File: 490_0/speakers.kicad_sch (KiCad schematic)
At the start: 14 parts, among them U1 MAX98357A, U2 MAX98357A

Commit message: Minor updates
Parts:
- renumbered FB1 to FB2, FB2 to FB3, R1 to R48, R2 to R49, U2 to U10, U1 to U9

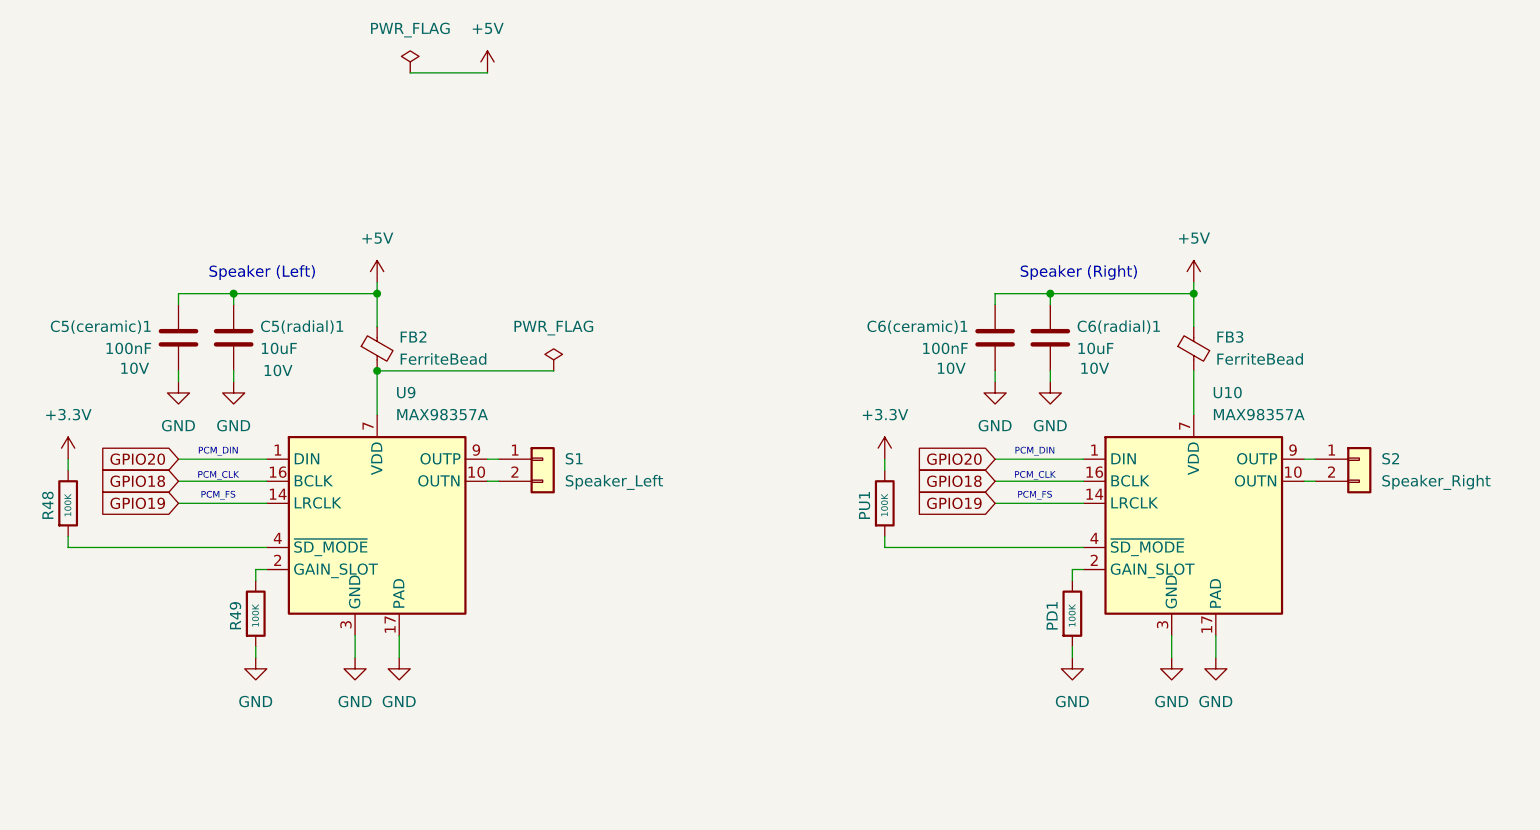
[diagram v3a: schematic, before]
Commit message: Updated box diagram
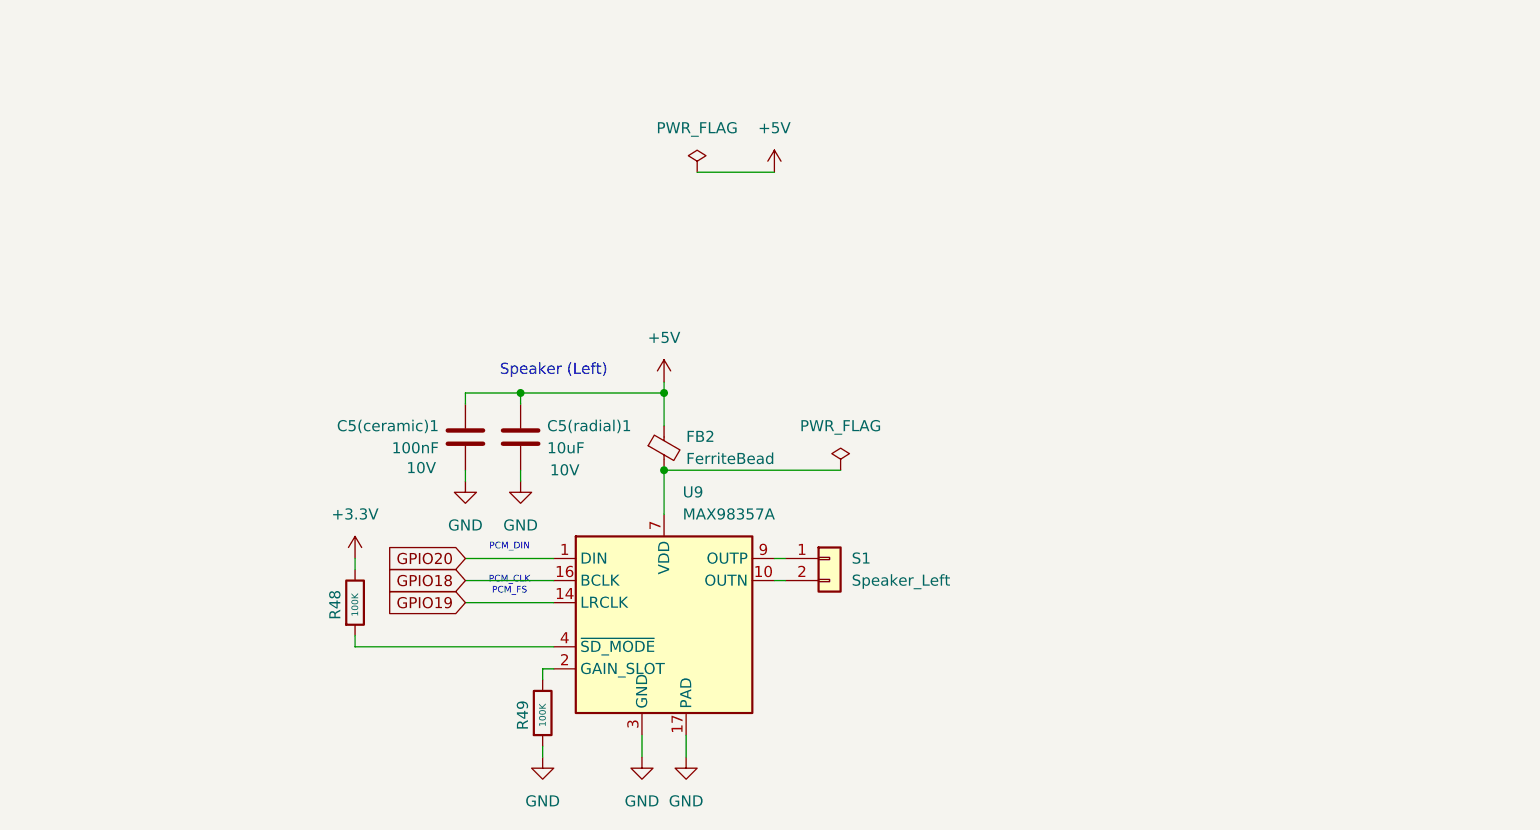
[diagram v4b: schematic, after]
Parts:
- removed C6(ceramic)1: 100nF, Capacitor_SMD:C_0603_1608Metric, symbol Device:C
- removed C6(radial)1: 10uF, Capacitor_THT:CP_Radial_D5.0mm_P2.50mm, symbol Device:C
- removed FB3: FerriteBead, Capacitor_SMD:C_0603_1608Metric, symbol Device:FerriteBead_Small
- removed PD1, PU1: 100K, symbol Device:R
- removed S2: Speaker_Right, Connector_JST:JST_PH_S2B-PH-K_1x02_P2.00mm_Horizontal, symbol Connector_Generic:Conn_01x02
- removed U10: MAX98357A, Package_DFN_QFN:TQFN-16-1EP_3x3mm_P0.5mm_EP1.23x1.23mm_ThermalVias, symbol Audio:MAX98357A
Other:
- note removed: "Speaker (Right)"
- moved on the sheet: C5(ceramic)1, C5(radial)1, FB2, R48, R49, S1, U9

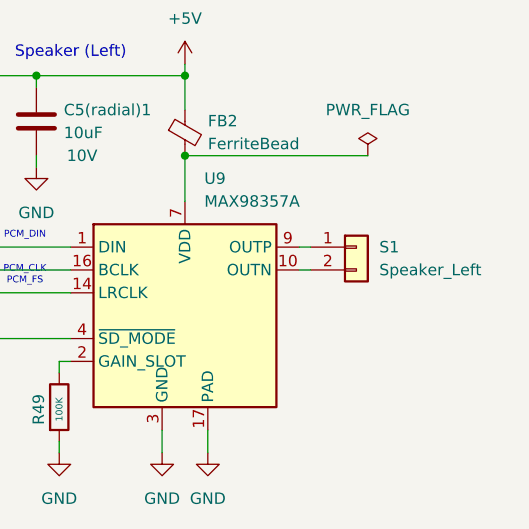
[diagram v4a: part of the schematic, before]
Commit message: BOM + ESD replacement for HDMI
Started BOM and changed ESD chips that were obsolete. Also added 2 pin connectors
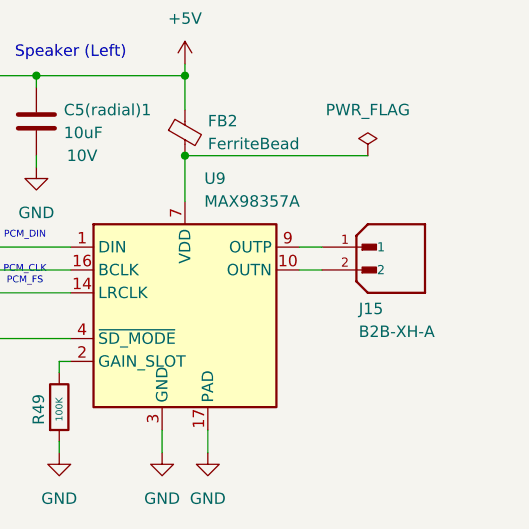
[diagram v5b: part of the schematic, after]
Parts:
- removed S1: Speaker_Left, Connector_JST:JST_PH_S2B-PH-K_1x02_P2.00mm_Horizontal, symbol Connector_Generic:Conn_01x02
- added J15: B2B-XH-A, B2B-XH-A:JST_B2B-XH-A, symbol capstone_parts:B2B-XH-A
- U9: Digikey Link (none) -> https://www.digikey.ca/en/products/detail/analog-devices-in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; Manufacturer (none) -> Analog Devices Inc./Maxim Integrated; Manufacturer Part (none) -> MAX98357AETE+T; Package (none) -> 16-WFQFN Exposed Pad; Price (none) -> 3.19; Supplier (none) -> DigiKey; Supplier P/N (none) -> MAX98357AETE+TCT-ND; Type (none) -> SMD; Unit (none) -> pcs; Voltage - Supply (none) -> 2.5V ~ 5.5V
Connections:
- net at U9.10 (OUTN): now also J15.2
- net at U9.9 (OUTP): now also J15.1

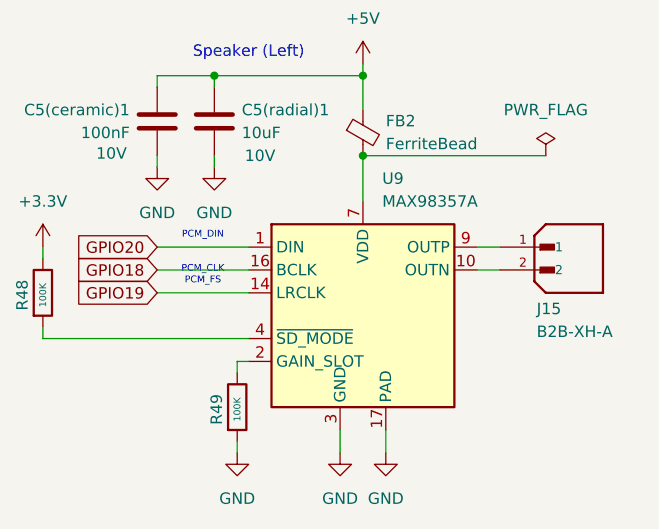
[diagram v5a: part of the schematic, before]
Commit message: Added another button + address fix
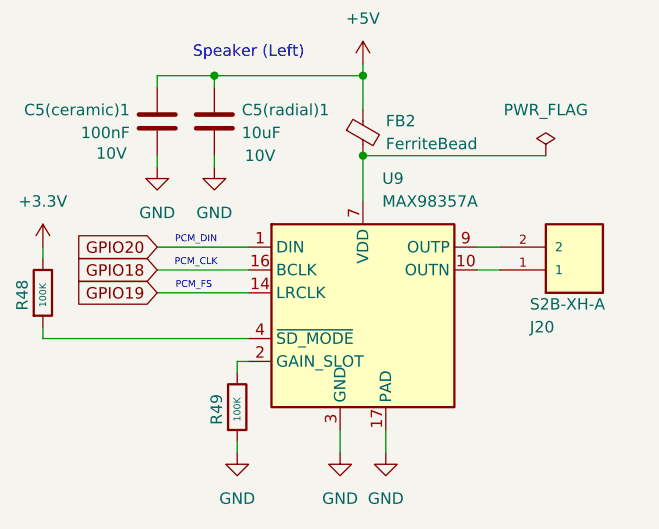
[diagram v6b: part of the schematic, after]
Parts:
- removed J15: B2B-XH-A, B2B-XH-A:JST_B2B-XH-A, symbol capstone_parts:B2B-XH-A
- added J20: S2B-XH-A, S2B-XH-A:JST_S2B-XH-A, symbol capstone_parts:S2B-XH-A
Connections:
- net at U9.9 (OUTP): now also J20.2
- net at U9.10 (OUTN): now also J20.1
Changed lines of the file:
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@@
 	(text "PCM_CLK"
 		(exclude_from_sim no)
-		(at 127 99.06 0)
+		(at 126.238 98.298 0)
 		(effects
 			(font
@@
 	(text "PCM_DIN"
 		(exclude_from_sim no)
-		(at 127 95.25 0)
+		(at 126.238 95.758 0)
 		(effects
 			(font
@@
 	(text "PCM_FS"
 		(exclude_from_sim no)
-		(at 127 100.33 0)
+		(at 125.984 100.838 0)
 		(effects
 			(font
@@
 	)
 	(symbol
+		(lib_id "capstone_parts:S2B-XH-A")
+		(at 172.72 96.52 0)
+		(mirror x)
+		(unit 1)
+		(exclude_from_sim no)
+		(in_bom yes)
+		(on_board yes)
+		(dnp no)
+		(property "Reference" "J20"
+			(at 163.322 105.41 0)
+			(effects
+				(font
+					(size 1.27 1.27)
+				)
+				(justify left)
+			)
+		)
+		(property "Value" "S2B-XH-A"
+			(at 163.322 102.87 0)
+			(effects
+				(font
+					(size 1.27 1.27)
+				)
+				(justify left)
+			)
+		)
+		(property "Footprint" "S2B-XH-A:JST_S2B-XH-A"
+			(at 172.72 96.52 0)
+			(effects
+				(font
+					(size 1.27 1.27)
+				)
+				(justify bottom)
+				(hide yes)
+			)
+		)
+		(property "Datasheet" "kicad-embed://B2B-XH-A 2 pin connector.pdf"
+			(at 172.72 96.52 0)
+			(effects
+				(font
+					(size 1.27 1.27)
+				)
+				(hide yes)
+			)
+		)
+		(property "Description" "CONN HEADER R/A 2POS 2.5MM"
+			(at 172.72 96.52 0)
+			(effects
+				(font
+					(size 1.27 1.27)
+				)
+				(hide yes)
+			)
+		)
+		(property "MANUFACTURER" "JST"
+			(at 172.72 96.52 0)
+			(effects
+				(font
+					(size 1.27 1.27)
+				)
+				(justify bottom)
+				(hide yes)
+			)
+		)
+		(property "Current - Load" "3A"
+			(at 172.72 96.52 0)
+			(effects
+				(font
+					(size 1.27 1.27)
+				)
+				(hide yes)
+			)
+		)
+		(property "Digikey Link" "https://www.digikey.ca/en/products/detail/jst-sales-america-inc/S2B-XH-A/1651055"
+			(at 172.72 96.52 0)
+			(effects
+				(font
+					(size 1.27 1.27)
+				)
+				(hide yes)
+			)
+		)
+		(property "Manufacturer" "JST Sales America Inc."
+			(at 172.72 96.52 0)
+			(effects
+				(font
+					(size 1.27 1.27)
+				)
+				(hide yes)
+			)
+		)
+		(property "Manufacturer Part" "S2B-XH-A"
+			(at 172.72 96.52 0)
+			(effects
+				(font
+					(size 1.27 1.27)
+				)
+				(hide yes)
+			)
+		)
+		(property "Package" "Bulk"
+			(at 172.72 96.52 0)
+			(effects
+				(font
+					(size 1.27 1.27)
+				)
+				(hide yes)
+			)
+		)
+		(property "Price" "0.12"
+			(at 172.72 96.52 0)
+			(effects
+				(font
+					(size 1.27 1.27)
+				)
+				(hide yes)
+			)
+		)
+		(property "Supplier" "DigiKey"
+			(at 172.72 96.52 0)
+			(effects
+				(font
+					(size 1.27 1.27)
+				)
+				(hide yes)
+			)
+		)
+		(property "Supplier P/N" "455-S2B-XH-A-ND"
+			(at 172.72 96.52 0)
+			(effects
+				(font
+					(size 1.27 1.27)
+				)
+				(hide yes)
+			)
+		)
+		(property "Type" "Through Hole, Right Angle"
+			(at 172.72 96.52 0)
+			(effects
+				(font
+					(size 1.27 1.27)
+				)
+				(hide yes)
+			)
+		)
+		(property "Unit" "pcs"
+			(at 172.72 96.52 0)
+			(effects
+				(font
+					(size 1.27 1.27)
+				)
+				(hide yes)
+			)
+		)
+		(property "Voltage - Load" "250V"
+			(at 172.72 96.52 0)
+			(effects
+				(font
+					(size 1.27 1.27)
+				)
+				(hide yes)
+			)
+		)
+		(pin "1"
+		)
+		(pin "2"
+		)
+		(instances
+			(project "490_0"
+				(path "/365a82ed-827d-43e1-aa2f-b98221c4179c/5522739b-0c93-41e1-a548-71dbce007147"
+					(reference "J20")
+					(unit 1)
+				)
+			)
+		)
+	)
+	(symbol
 		(lib_id "Device:C")
 		(at 128.27 82.55 0)
@@
 					(unit 1)
 				)
-			)
-		)
-	)
-	(symbol
-		(lib_id "capstone_parts:B2B-XH-A")
-		(at 167.64 99.06 0)
-		(unit 1)
-		(exclude_from_sim no)
-		(in_bom yes)
-		(on_board yes)
-		(dnp no)
-		(property "Reference" "J15"
-			(at 164.084 103.378 0)
-			(effects
-				(font
-					(size 1.27 1.27)
-				)
-				(justify left)
-			)
-		)
-		(property "Value" "B2B-XH-A"
-			(at 164.084 105.918 0)
-			(effects
-				(font
-					(size 1.27 1.27)
-				)
-				(justify left)
-			)
-		)
-		(property "Footprint" "B2B-XH-A:JST_B2B-XH-A"
-			(at 167.64 99.06 0)
-			(effects
-				(font
-					(size 1.27 1.27)
-				)
-				(justify bottom)
-				(hide yes)
-			)
-		)
-		(property "Datasheet" "kicad-embed://B2B-XH-A 2 pin connector.pdf"
-			(at 167.64 99.06 0)
-			(effects
-				(font
-					(size 1.27 1.27)
-				)
-				(hide yes)
-			)
-		)
-		(property "Description" "CONN HEADER VERT 2POS 2.5MM"
-			(at 167.64 99.06 0)
-			(effects
-				(font
-					(size 1.27 1.27)
-				)
-				(hide yes)
-			)
-		)
-		(property "PARTREV" "N/A"
-			(at 167.64 99.06 0)
-			(effects
-				(font
-					(size 1.27 1.27)
-				)
-				(justify bottom)
-				(hide yes)
-			)
-		)
-		(property "STANDARD" "Manufacturer Recommendations"
-			(at 167.64 99.06 0)
-			(effects
-				(font
-					(size 1.27 1.27)
-				)
-				(justify bottom)
-				(hide yes)
-			)
-		)
-		(property "MAXIMUM_PACKAGE_HEIGHT" "7 mm"
-			(at 167.64 99.06 0)
-			(effects
-				(font
-					(size 1.27 1.27)
-				)
-				(justify bottom)
-				(hide yes)
-			)
-		)
-		(property "MANUFACTURER" "JST Sales America Inc."
-			(at 167.64 99.06 0)
-			(effects
-				(font
-					(size 1.27 1.27)
-				)
-				(justify bottom)
-				(hide yes)
-			)
-		)
-		(property "Current - Load" "3A"
-			(at 167.64 99.06 0)
-			(effects
-				(font
-					(size 1.27 1.27)
-				)
-				(hide yes)
-			)
-		)
-		(property "Digikey Link" "https://www.digikey.ca/en/products/detail/jst-sales-america-inc/B2B-XH-A/1651045"
-			(at 167.64 99.06 0)
-			(effects
-				(font
-					(size 1.27 1.27)
-				)
-				(hide yes)
-			)
-		)
-		(property "Manufacturer" "JST Sales America Inc."
-			(at 167.64 99.06 0)
-			(effects
-				(font
-					(size 1.27 1.27)
-				)
-				(hide yes)
-			)
-		)
-		(property "Manufacturer Part" "B2B-XH-A"
-			(at 167.64 99.06 0)
-			(effects
-				(font
-					(size 1.27 1.27)
-				)
-				(hide yes)
-			)
-		)
-		(property "Package" "Bulk"
-			(at 167.64 99.06 0)
-			(effects
-				(font
-					(size 1.27 1.27)
-				)
-				(hide yes)
-			)
-		)
-		(property "Price" "0.10"
-			(at 167.64 99.06 0)
-			(effects
-				(font
-					(size 1.27 1.27)
-				)
-				(hide yes)
-			)
-		)
-		(property "Supplier" "DigiKey"
-			(at 167.64 99.06 0)
-			(effects
-				(font
-					(size 1.27 1.27)
-				)
-				(hide yes)
-			)
-		)
-		(property "Supplier P/N" "455-B2B-XH-A-ND"
-			(at 167.64 99.06 0)
-			(effects
-				(font
-					(size 1.27 1.27)
-				)
-				(hide yes)
-			)
-		)
-		(property "Type" "Through Hole"
-			(at 167.64 99.06 0)
-			(effects
-				(font
-					(size 1.27 1.27)
-				)
-				(hide yes)
-			)
-		)
-		(property "Unit" "pcs"
-			(at 167.64 99.06 0)
-			(effects
-				(font
-					(size 1.27 1.27)
-				)
-				(hide yes)
-			)
-		)
-		(property "Voltage - Load" "250V"
-			(at 167.64 99.06 0)
-			(effects
-				(font
-					(size 1.27 1.27)
-				)
-				(hide yes)
-			)
-		)
-		(pin "2"
-		)
-		(pin "1"
-		)
-		(instances
-			(project "490_0"
-				(path "/365a82ed-827d-43e1-aa2f-b98221c4179c/5522739b-0c93-41e1-a548-71dbce007147"
-					(reference "J15")
-					(unit 1)
-				)
